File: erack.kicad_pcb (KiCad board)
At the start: 2 copper layers, 68.8 x 100 mm, 0 parts

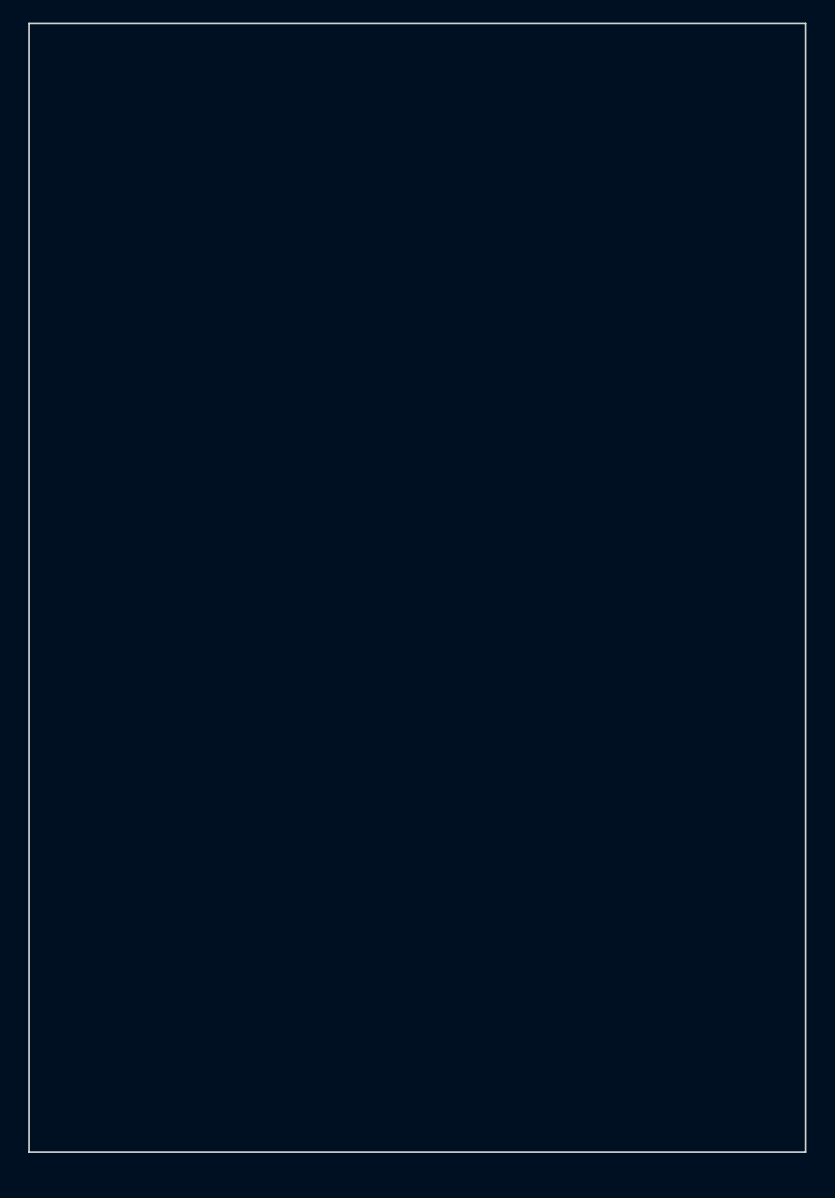
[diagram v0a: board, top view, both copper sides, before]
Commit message: Fix some bad dimensions
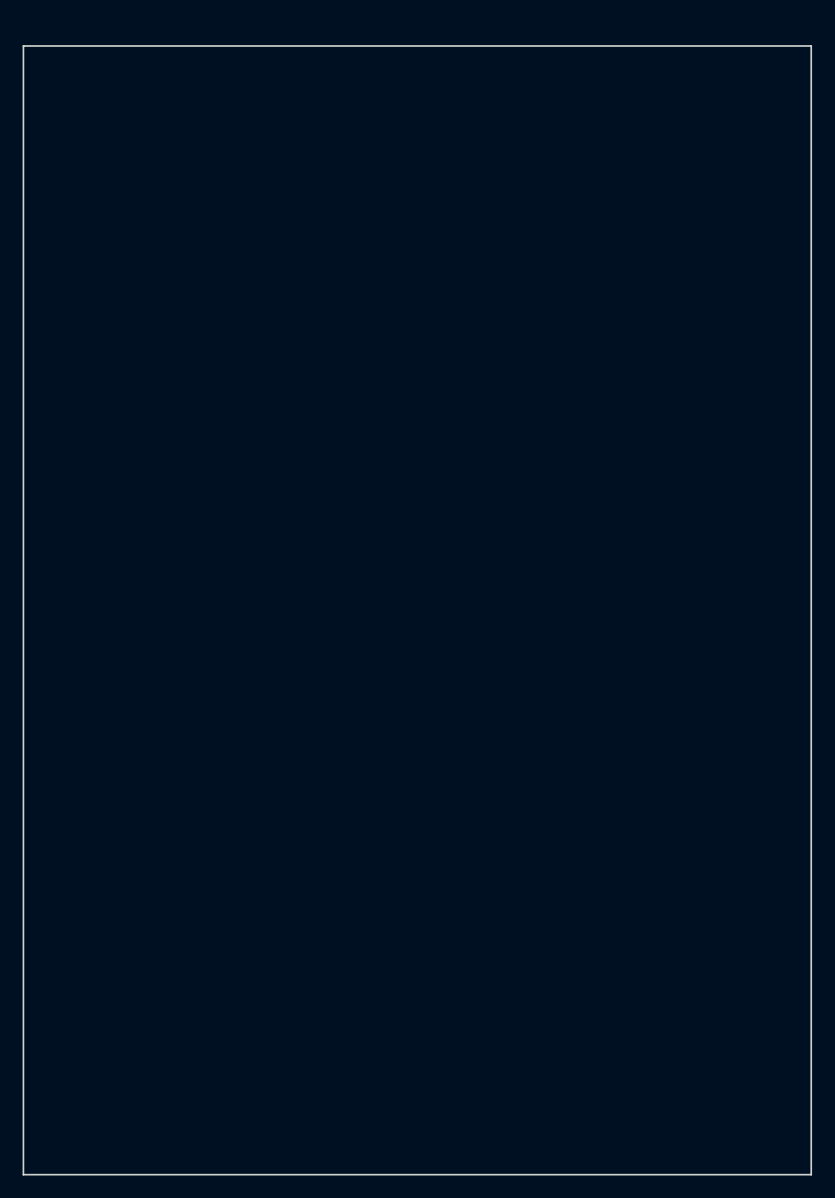
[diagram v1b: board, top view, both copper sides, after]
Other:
- board size 68.8 x 100 mm -> 69.8 x 100 mm

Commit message: Starting to standardize a few things
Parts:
- added REF**: Socket_Strip_Straight_1x39_Pitch2.54mm, erack:PinSocket39, B.Cu at (117.0, 39.8)
- added REF**: Val**, erack:PinSocket39_M, B.Cu at (183.8, 39.8)
